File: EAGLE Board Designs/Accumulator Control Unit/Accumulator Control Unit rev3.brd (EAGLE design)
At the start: 186.7 x 135.7 mm, 237 parts, among them J1 CONNECTOR-CAN_μF_S_RA_, J2 CONNECTOR-8_MF_T_V_, J3 CONNECTOR-8_S_S, J4 CONNECTOR-2_MF_T_V_, J5 CONNECTOR-12_MF_T_V_, J6 CONNECTOR-14_MF_T_V_, J7 JUMPER_0603_, Q1 TRANSISTOR_N_MOS__PMV15ENEA, Q2 TRANSISTOR_N_MOS__PMV15ENEA, Q3 TRANSISTOR_N_MOS__PMV15ENEA, Q4 TRANSISTOR_N_MOS__PMV15ENEA, T1 TRANSFORMER_HM2112ZNLT_AIRGAP, U1 RELAY_SOLIDSTATE_NO, U10 OPAMP_1_CHANNEL_OPA991, U11 LOGICGATE_AND_DCK3, U12 OPAMP_1_CHANNEL_OPA991, U13 OPAMP_1_CHANNEL_OPA991, U14 OPAMP_1_CHANNEL_OPA991, U15 LOGICGATE_AND_DCK3, U16 RELAY_SOLIDSTATE_NO, U17 VOLTAGE_REGULATOR_SOT223_3.3V, U18 OPAMP_1_CHANNEL_OPA991, U19 MAX7404, U2 ADG1423, U20 OPAMP_1_CHANNEL_OPA991, U21 LOGICGATE_BUFFER, U22 OPAMP_1_CHANNEL_OPA991, U25 TCAN1051HQV-Q1, U26 MAX7404, U27 OPAMP_1_CHANNEL_OPA991, U28 MAX7404, U29 OPAMP_1_CHANNEL_OPA991, U3 LM555, U30 MAX7404, U4 OPAMP_1_CHANNEL_OPA991, U40 RELAY_SOLIDSTATE_NO, U5 LTC6820, U6 ADM8316WBX30, U7 OPAMP_1_CHANNEL_OPA991, U8 LOGICGATE_AND_DCK3, U9 OPAMP_1_CHANNEL_OPA991

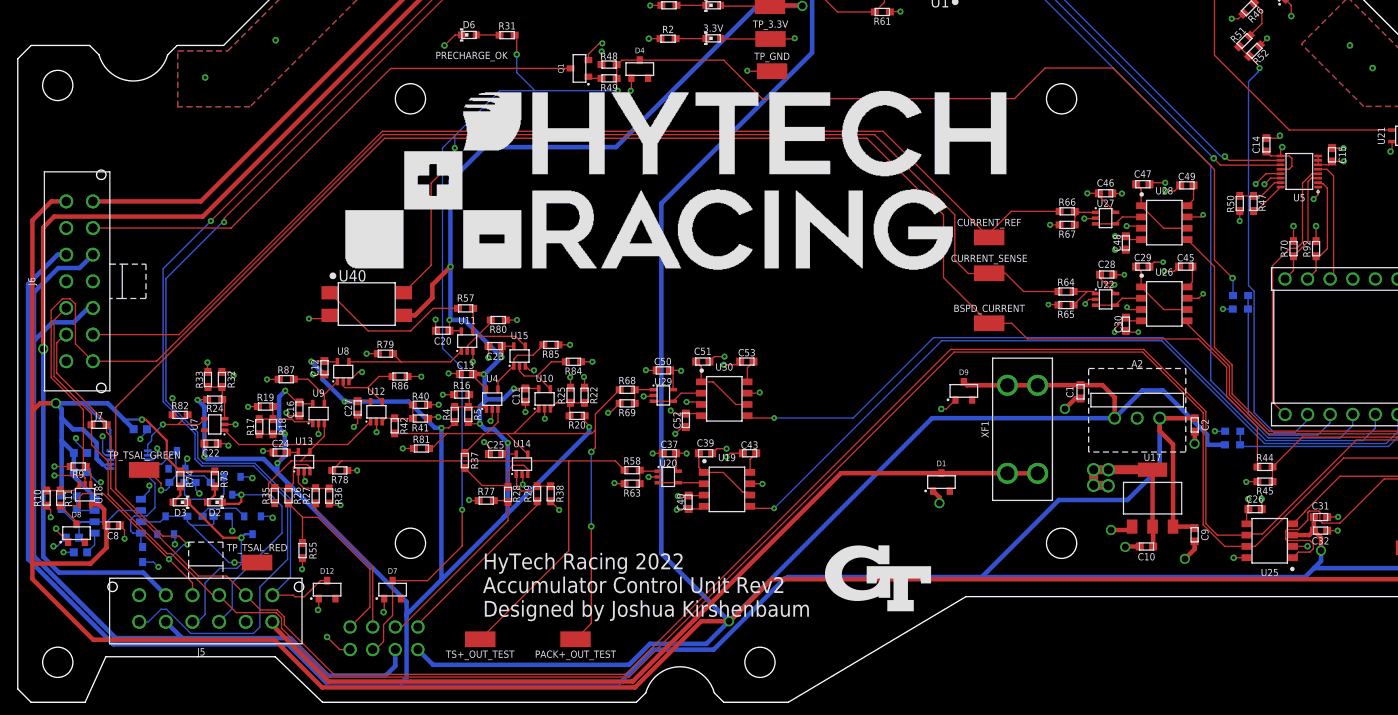
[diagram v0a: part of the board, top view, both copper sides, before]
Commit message: can jumper, tsal fuse
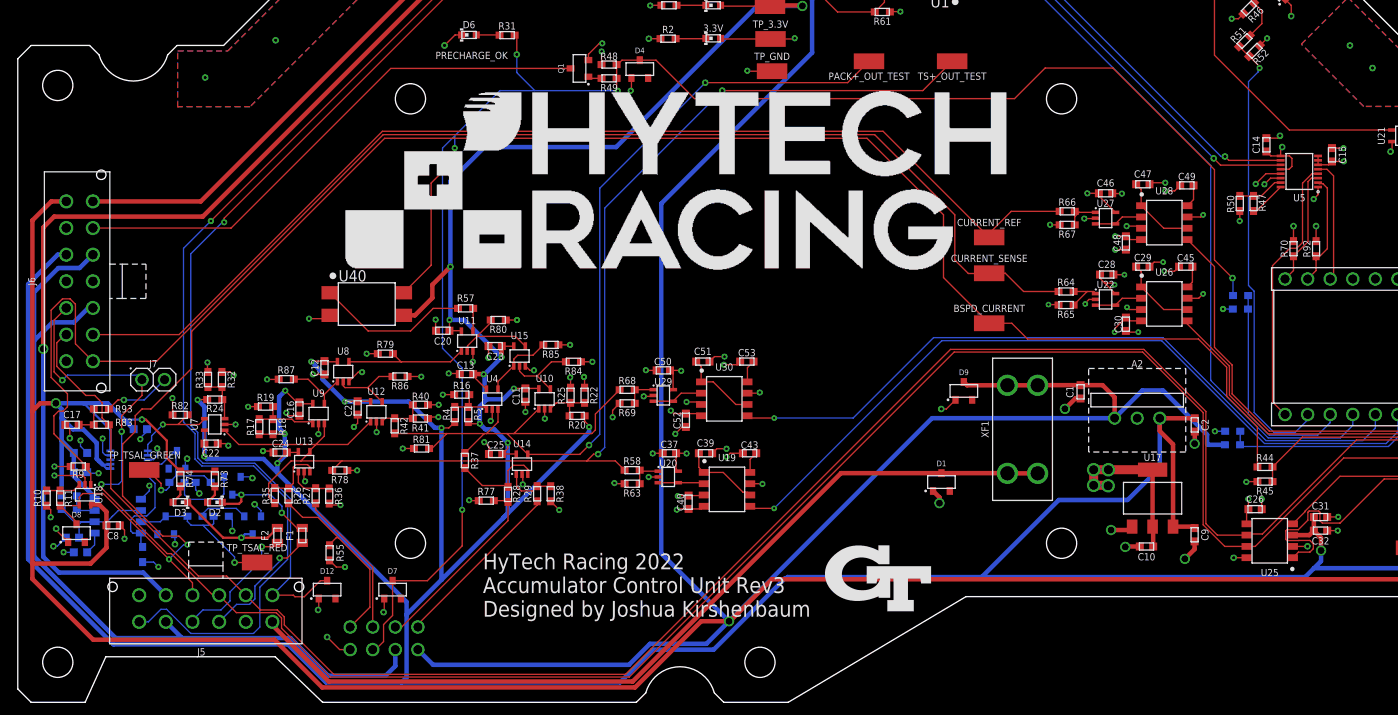
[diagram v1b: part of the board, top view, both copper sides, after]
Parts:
- added C17: CAPACITOR_0603_10V_4.7NF, HyTechDevices:0603-CAP
- added F1, F2: FUSE_0603_.75A, HyTechDevices:0603-FUSE
- added R83, R93: RESISTOR_0603_60.4, HyTechDevices:0603-RES
- J7: value JUMPER_0603_ -> JUMPER__1X02; device HyTechDevices:0603-RES -> HyTechDevices:1X02
- R14, R30, R39, R44, R51: value RESISTOR_0603_33K -> RESISTOR_0603_
- moved TS+_OUT_TEST 83.9 mm to (105.1, 70.6)
- moved PACK+_OUT_TEST 72.9 mm to (95.8, 70.6)
- moved J7 7.94 mm to (15.2, 34.8)
- moved R55 3.06 mm to (35.1, 15.3)
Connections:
- new net CANH/1.3B: J7.2, R93.2
- new net N$21: C17.2, R83.1, R93.1
- new net N$28: F1.1, J5.3
- new net N$31: F2.1, J5.4
- net CANL: now also R83.2; no longer J7.2
- net GND: now also C17.1
- net TSAL_GREEN: now also F1.2; no longer J5.3
- net TSAL_RED: now also F2.2; no longer J5.4
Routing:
- net TS+_OUT: track 93.2 -> 144.5 mm, vias 0 -> 2
- net PACK+_OUT: track 69.2 -> 117.7 mm
- net N$31: track 0.00 -> 14.8 mm, vias 0 -> 1
- net N$28: track 0.00 -> 14.1 mm, vias 0 -> 1
- net TSAL_GREEN: track 25.2 -> 13.0 mm, vias 1 -> 2
- net CANH: track 219.4 -> 230.1 mm, vias 0 -> 3
- net TSAL_RED: track 22.3 -> 13.6 mm
- net CANH/1.3B: track 0.00 -> 7.63 mm, vias 0 -> 1
- net N$21: track 0.00 -> 3.48 mm
- net IMD_OK: track 179.2 -> 176.9 mm
- net AMS_OK: track 216.0 -> 214.1 mm
- net CURRENT: track 161.7 -> 163.3 mm
- net GND: track 225.7 -> 227.2 mm, vias 164 -> 165
- net ISO_TS-: track 22.5 -> 21.0 mm
- net N$19: track 19.2 -> 18.3 mm
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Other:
- board text added: "HyTech Racing 2022 Accumulator Control Unit Rev3 Designed by Joshua Kirshenbaum"
- board text removed: "HyTech Racing 2022 Accumulator Control Unit Rev2 Designed by Joshua Kirshenbaum"

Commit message: fix text
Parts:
- removed D6: LED_0603_RED, HyTechDevices:0603-LED
- added PRECHARGE_OK: LED_0603_RED, HyTechDevices:0603-LED
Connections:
- net GND: now also PRECHARGE_OK.1; no longer D6.1
- net N$4: now also PRECHARGE_OK.2; no longer D6.2
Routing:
- net N$4: track 2.63 -> 4.41 mm
- net GND: track 227.2 -> 228.3 mm, vias 165 -> 145
- removed copper zone on layer 16, net GND
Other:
- board text removed: "PRECHARGE_OK"
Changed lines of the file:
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@@
 Accumulator Control Unit Rev3
 Designed by Joshua Kirshenbaum</text>
-<text x="46.99" y="70.866" size="0.8128" layer="25" font="vector" ratio="16">PRECHARGE_OK</text>
 </plain>
 <attributes>
@@
 <attribute name="VOLTAGE" value="8V" x="111.88109375" y="-5.19748125" size="1.778" layer="27" display="off"/>
 </element>
-<element name="D6" library="HyTechDevices" package="0603-LED" value="LED_0603_RED" x="50.75510625" y="73.57428125" smashed="yes">
-<attribute name="COLOR" value="Red" x="92.66510625" y="-14.05571875" size="1.778" layer="27" display="off"/>
-<attribute name="DKPN" value="754-1786-1-ND" x="92.66510625" y="-14.05571875" size="1.778" layer="27" display="off"/>
-<attribute name="MANUFACTURER" value="Kingbright" x="92.66510625" y="-14.05571875" size="1.778" layer="27" display="off"/>
-<attribute name="MOPN" value="604-APT1608SECKJ3PRV" x="92.66510625" y="-14.05571875" size="1.778" layer="27" display="off"/>
-<attribute name="MPN" value="APT1608SECK/J3-PRV" x="92.66510625" y="-14.05571875" size="1.778" layer="27" display="off"/>
-<attribute name="NAME" x="50.75510625" y="74.32428125" size="0.8128" layer="25" font="vector" align="bottom-center"/>
+<element name="PRECHARGE_OK" library="HyTechDevices" package="0603-LED" value="LED_0603_RED" x="48.97710625" y="73.57428125" smashed="yes">
+<attribute name="COLOR" value="Red" x="90.88710625" y="-14.05571875" size="1.778" layer="27" display="off"/>
+<attribute name="DKPN" value="754-1786-1-ND" x="90.88710625" y="-14.05571875" size="1.778" layer="27" display="off"/>
+<attribute name="MANUFACTURER" value="Kingbright" x="90.88710625" y="-14.05571875" size="1.778" layer="27" display="off"/>
+<attribute name="MOPN" value="604-APT1608SECKJ3PRV" x="90.88710625" y="-14.05571875" size="1.778" layer="27" display="off"/>
+<attribute name="MPN" value="APT1608SECK/J3-PRV" x="90.88710625" y="-14.05571875" size="1.778" layer="27" display="off"/>
+<attribute name="NAME" x="48.97710625" y="74.32428125" size="0.8128" layer="25" font="vector" align="bottom-center"/>
 </element>
 <element name="J1" library="HyTechDevices" package="MOLEX_MICROFIT_SMD_RIGHTANGLE_04_DUAL" value="CONNECTOR-CAN_μF_S_RA_" x="162.12229375" y="15.88451875" smashed="yes">
@@
 <attribute name="MOPN" value="603-RC0603FR-071KL" x="70.28770625" y="-21.70111875" size="1.778" layer="27" display="off"/>
 <attribute name="MPN" value="RC0603FR-071KL" x="70.28770625" y="-21.70111875" size="1.778" layer="27" display="off"/>
-<attribute name="NAME" x="55.04770625" y="74.18388125" size="0.8128" layer="25" font="vector" align="bottom-center"/>
+<attribute name="NAME" x="55.04770625" y="74.43788125" size="0.8128" layer="25" font="vector" align="bottom-center"/>
 <attribute name="POWER" value="0.1W" x="70.28770625" y="-21.70111875" size="1.778" layer="27" display="off"/>
 <attribute name="RESISTANCE" value="1k" x="70.28770625" y="-21.70111875" size="1.778" layer="27" display="off"/>
@@
 <contactref element="C20" pad="2"/>
 <contactref element="U11" pad="3"/>
-<contactref element="D6" pad="1"/>
+<contactref element="PRECHARGE_OK" pad="1"/>
 <contactref element="Q1" pad="2"/>
 <contactref element="D4" pad="1"/>
@@
 <vertex x="17.9832" y="65.4304"/>
 </polygon>
-<polygon width="0.1524" layer="16">
-<vertex x="40.386" y="125.3744"/>
-<vertex x="46.5328" y="125.3744"/>
-<vertex x="46.5582" y="125.349"/>
-<vertex x="46.5582" y="85.9282"/>
-<vertex x="26.1366" y="65.5066"/>
-<vertex x="17.9832" y="65.5066"/>
-<vertex x="17.9832" y="71.7804"/>
-<vertex x="23.622" y="71.7804"/>
-<vertex x="40.6908" y="88.8492"/>
-<vertex x="40.6908" y="125.0696"/>
-</polygon>
 <polygon width="0.1524" layer="1" isolate="0.3048">
 <vertex x="170.673" y="71.628"/>
@@
 <vertex x="155.8036" y="71.628"/>
 </polygon>
-<polygon width="0.1524" layer="16" isolate="0.3048">
-<vertex x="149.6314" y="77.7748"/>
-<vertex x="155.7782" y="71.628"/>
-<vertex x="170.6984" y="71.628"/>
-<vertex x="170.6984" y="65.532"/>
-<vertex x="151.4094" y="65.532"/>
-<vertex x="144.399" y="72.5424"/>
-</polygon>
 <polygon width="0.1524" layer="1" isolate="0.3048">
 <vertex x="185.4454" y="64.0588"/>
@@
 <vertex x="185.4454" y="18.3642"/>
 </polygon>
-<via x="43.4848" y="123.3678" extent="1-16" drill="0.35"/>
-<via x="43.6372" y="112.1664" extent="1-16" drill="0.35"/>
-<via x="43.6372" y="103.6066" extent="1-16" drill="0.35"/>
-<via x="43.7134" y="95.123" extent="1-16" drill="0.35"/>
-<via x="42.9768" y="87.63" extent="1-16" drill="0.35"/>
-<via x="36.6776" y="80.5942" extent="1-16" drill="0.35"/>
-<via x="29.0068" y="72.9742" extent="1-16" drill="0.35"/>
-<via x="21.082" y="68.7832" extent="1-16" drill="0.35"/>
-<via x="149.86" y="72.39" extent="1-16" drill="0.35"/>
-<via x="152.4" y="69.85" extent="1-16" drill="0.35"/>
-<via x="156.21" y="68.58" extent="1-16" drill="0.35"/>
-<via x="161.29" y="68.58" extent="1-16" drill="0.35"/>
-<via x="166.37" y="68.58" extent="1-16" drill="0.35"/>
-<polygon width="0.1524" layer="16" isolate="0.3048">
-<vertex x="185.4454" y="64.0588"/>
-<vertex x="185.4454" y="18.3388"/>
-<vertex x="178.2318" y="18.3388"/>
-<vertex x="178.2318" y="64.0588"/>
-</polygon>
-<via x="182.1942" y="60.452" extent="1-16" drill="0.35"/>
-<via x="182.3212" y="54.4322" extent="1-16" drill="0.35"/>
-<via x="182.5498" y="47.9298" extent="1-16" drill="0.35"/>
-<via x="182.4228" y="41.4528" extent="1-16" drill="0.35"/>
-<via x="182.4228" y="35.306" extent="1-16" drill="0.35"/>
-<via x="182.1942" y="29.3878" extent="1-16" drill="0.35"/>
-<via x="182.3212" y="23.0124" extent="1-16" drill="0.35"/>
 <contactref element="R84" pad="1"/>
 <contactref element="R85" pad="1"/>
@@
 <wire x1="41.2242" y1="8.7122" x2="41.148" y2="8.636" width="0.1524" layer="1"/>
 <via x="41.148" y="8.636" extent="1-16" drill="0.35"/>
-<wire x1="48.006" y1="72.39" x2="49.19028125" y2="73.57428125" width="0.1524" layer="1"/>
-<via x="48.006" y="72.39" extent="1-16" drill="0.35"/>
-<wire x1="49.19028125" y1="73.57428125" x2="49.93010625" y2="73.57428125" width="0.1524" layer="1"/>
+<wire x1="45.212" y1="72.136" x2="46.65028125" y2="73.57428125" width="0.1524" layer="1"/>
+<via x="45.212" y="72.136" extent="1-16" drill="0.35"/>
+<wire x1="46.65028125" y1="73.57428125" x2="48.15210625" y2="73.57428125" width="0.1524" layer="1"/>
 <contactref element="C17" pad="1"/>
 <wire x1="5.346" y1="29.718" x2="5.852365625" y2="29.211634375" width="0.1524" layer="1"/>
@@
 <signal name="N$4">
 <contactref element="R31" pad="1"/>
-<contactref element="D6" pad="2"/>
-<wire x1="51.58010625" y1="73.57428125" x2="54.17230625" y2="73.57428125" width="0.1524" layer="1"/>
+<contactref element="PRECHARGE_OK" pad="2"/>
+<wire x1="49.80210625" y1="73.57428125" x2="54.17230625" y2="73.57428125" width="0.1524" layer="1"/>
 <wire x1="54.17230625" y1="73.57428125" x2="54.19770625" y2="73.54888125" width="0.1524" layer="1"/>
 </signal>

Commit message: some changes based on checklist
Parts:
- removed C35: CAPACITOR_0603_10V_0.1UF, HyTechDevices - Copy:0603-CAP
- removed R13: RESISTOR_0603_100K, HyTechDevices - Copy:0603-RES
- removed R59: RESISTOR_0603_10K, HyTechDevices:0603-RES
- removed U$3: (no value), HyTechAesthetics:TS
- added PRECHARGE_OK_TEST: TEST_POINT, HyTechDevices - Copy:MICRO_MINIATURE
- added R94: RESISTOR_0603_10K, HyTechDevices:0603-RES
- added U$2: (no value), HyTechAesthetics:HV_0.50"
- R53: value RESISTOR_0603_100 -> RESISTOR_0603_120
- moved U$12 16.5 mm to (100.9, 16.4)
- moved U$18 16.5 mm to (100.9, 66.4)
- moved PACK+_OUT_TEST 2.03 mm to (93.7, 70.6)
- moved C36 1.78 mm to (161.5, 62.1)
- moved R55 0.66 mm to (35.1, 16.0), turned to 0 degrees
- renumbered D2 to TSAL_GREEN, D3 to TSAL_RED
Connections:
- removed net N$15: R13.2, U21.2, U6.1
- net +3V3: no longer C35.1, U6.5
- net AMS_OK_3.3V: now also U6.1; no longer U21.4
- net GND: no longer C35.2, R13.1, R59.1
- net PRECHARGE_OK: now also PRECHARGE_OK_TEST.1
- net TEENSY_OK: now also R94.1, R94.2, U6.5; no longer R59.2
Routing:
- net TEENSY_OK: track 30.8 -> 52.3 mm
- net N$15: track 19.6 -> 0.00 mm
- net AMS_OK_3.3V: track 60.9 -> 78.8 mm, vias 0 -> 2
- net PRECHARGE_OK: track 207.0 -> 216.6 mm
- net GND: track 228.3 -> 223.7 mm, vias 145 -> 142
- net +3V3: track 86.6 -> 82.5 mm, vias 25 -> 24
- net PACK+_OUT: track 117.7 -> 115.7 mm
- removed copper zone on layer 1, net GND

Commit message: passed review
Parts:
- removed C40, C47, C48, C51: CAPACITOR_0603_10V_0.1UF, HyTechDevices - Copy:0603-CAP
- removed C43, C45, C49, C53: CAPACITOR_0603_10V_680PF, HyTechDevices - Copy:0603-CAP
- removed C46, C50: CAPACITOR_0603_25V_0.1UF, HyTechDevices:0603-CAP
- removed D12: TVS_15V, HyTechDevices:SOT-23
- removed J7: JUMPER__1X02, HyTechDevices:1X02
- removed R82, R84, R85, R86, R87: RESISTOR_0603_10K, HyTechDevices - Copy:0603-RES
- removed R83, R93: RESISTOR_0603_60.4, HyTechDevices:0603-RES
- removed R92: RESISTOR_0603_2K, HyTechDevices:0603-RES
- removed R94: RESISTOR_0603_10K, HyTechDevices:0603-RES
- removed U$21, U$22: (no value), HyTechManufacturing:MOUNTING_M3
- removed U28, U30: MAX7404, HyTechDevices:SOIC-08(NARROW,0.15")
- removed U29: OPAMP_1_CHANNEL_OPA991, HyTechDevices:SC-70-5
- removed U40: RELAY_SOLIDSTATE_NO, HyTechDevices:DIP-4
- added C100: CAPACITOR_0603_10V_10NF, HyTechDevices - Copy:0603-CAP
- added C101: CAPACITOR_0603_25V_1UF, HyTechDevices - Copy:0603-CAP
- added C102: CAPACITOR_0603_25V_0.1UF, HyTechDevices - Copy:0603-CAP
- added C103: CAPACITOR_0603_10V_4.7UF, HyTechDevices - Copy:0603-CAP
- added C104: CAPACITOR_0603_25V_1UF, HyTechDevices:0603-CAP
- added C18, C19, C34, C38: CAPACITOR_0603_10V_0.1UF, HyTechDevices:0603-CAP
- added C35: CAPACITOR_0603_25V_0.1UF, HyTechDevices:0603-CAP
- added D3: TVS_15V, HyTechDevices:SOT-23
- added J100: CONNECTOR-8_S_S, HyTechDevices:FLEX_STACK_PTH_08_DUAL
- added R100, R59: RESISTOR_0603_10K, HyTechDevices - Copy:0603-RES
- added R105: RESISTOR_0603_43K, HyTechDevices:0603-RES
- added R106: RESISTOR_0603_1K, HyTechDevices:0603-RES
- added R107: RESISTOR_0603_12K, HyTechDevices - Copy:0603-RES
- added R108, R110: RESISTOR_0603_, HyTechDevices:0603-RES
- added R109: RESISTOR_0603_18.7K, HyTechDevices:0603-RES
- added R13: RESISTOR_0603_10, HyTechDevices:0603-RES
- added U$100: (no value), HyTechManufacturing:HV_LARGE
- added U$3: (no value), HyTechAesthetics:TS
- added U100: ADG1423, HyTechDevices:MSOP-10
- added U101: LM555, HyTechDevices:SOIC-08(NARROW,0.15")
- added U23, U24: OPAMP_1_CHANNEL_OPA991, HyTechDevices:SC-70-5
- A1: value TEENSY_4.0 -> VOLTAGE_REGULATOR_MODULE_OKI-78SR_5V; device HyTechDevices:TEENSY_SHORT -> HyTechDevices - Copy:OKI-78SR
- A2: value VOLTAGE_REGULATOR_MODULE_OKI-78SR_5V -> TEENSY_4.0; device HyTechDevices - Copy:OKI-78SR -> HyTechDevices:TEENSY_SHORT
- C1: value CAPACITOR_0603_25V_10UF -> CAPACITOR_0603_10V_10NF; device HyTechDevices:0603-CAP -> HyTechDevices - Copy:0603-CAP
- C10: value CAPACITOR_0603_10V_4.7UF -> CAPACITOR_0603_10V_0.1UF
- C11, C22, C31: device HyTechDevices:0603-CAP -> HyTechDevices - Copy:0603-CAP
- C12, C23: value CAPACITOR_0603_10V_0.1UF -> CAPACITOR_0603_10V_680PF; device HyTechDevices:0603-CAP -> HyTechDevices - Copy:0603-CAP
- C15: value CAPACITOR_0603_10V_10NF -> CAPACITOR_0603_10V_0.1UF
- C17: value CAPACITOR_0603_10V_4.7NF -> CAPACITOR_0603_10V_0.1UF
- C2: value CAPACITOR_0603_25V_10UF -> CAPACITOR_0603_25V_0.1UF
- C20: value CAPACITOR_0603_10V_0.1UF -> CAPACITOR_0603_25V_0.1UF
- C24: value CAPACITOR_0603_10V_0.1UF -> CAPACITOR_0603_25V_10UF
- C25: value CAPACITOR_0603_10V_0.1UF -> CAPACITOR_0603_10V_4.7NF
- C28, C7: value CAPACITOR_0603_25V_0.1UF -> CAPACITOR_0603_10V_0.1UF
- C29: value CAPACITOR_0603_10V_0.1UF -> CAPACITOR_0603_25V_0.1UF; device HyTechDevices - Copy:0603-CAP -> HyTechDevices:0603-CAP
- C3: value CAPACITOR_0603_25V_1UF -> CAPACITOR_0603_10V_0.1UF; device HyTechDevices:0603-CAP -> HyTechDevices - Copy:0603-CAP
- C32: value CAPACITOR_0603_10V_1UF -> CAPACITOR_0603_10V_680PF; device HyTechDevices:0603-CAP -> HyTechDevices - Copy:0603-CAP
- C33: value CAPACITOR_0603_10V_10NF -> CAPACITOR_0603_25V_10UF; device HyTechDevices - Copy:0603-CAP -> HyTechDevices:0603-CAP
- C36: value CAPACITOR_0603_10V_0.1UF -> CAPACITOR_0603_10V_4.7UF
- C37: value CAPACITOR_0603_25V_0.1UF -> CAPACITOR_0603_10V_1UF; device HyTechDevices:0603-CAP -> HyTechDevices - Copy:0603-CAP
- C39: value CAPACITOR_0603_10V_0.1UF -> CAPACITOR_0603_10V_1UF; device HyTechDevices - Copy:0603-CAP -> HyTechDevices:0603-CAP
- C4: value CAPACITOR_0603_10V_10NF -> CAPACITOR_0603_10V_680PF
- C5: value CAPACITOR_0603_10V_4.7UF -> CAPACITOR_0603_10V_0.1UF; device HyTechDevices - Copy:0603-CAP -> HyTechDevices:0603-CAP
- C6: value CAPACITOR_0603_25V_1UF -> CAPACITOR_0603_10V_10NF; device HyTechDevices - Copy:0603-CAP -> HyTechDevices:0603-CAP
- C9: value CAPACITOR_0603_10V_1UF -> CAPACITOR_0603_10V_0.1UF
- D1: value TVS_15V -> LED_0603_YELLOW; device HyTechDevices:SOT-23 -> HyTechDevices - Copy:0603-LED
- D10: value LED_0603_GREEN -> TVS_15V; device HyTechDevices:0603-LED -> HyTechDevices:SOT-23
- D11: value LED_0603_YELLOW -> TVS_15V; device HyTechDevices - Copy:0603-LED -> HyTechDevices:SOT-23
- D5: value TVS_15V -> LED_0603_GREEN; device HyTechDevices:SOT-23 -> HyTechDevices:0603-LED
- J1: value CONNECTOR-CAN_μF_S_RA_ -> CONNECTOR-2_MF_T_V_; device HyTechDevices:MOLEX_MICROFIT_SMD_RIGHTANGLE_04_DUAL -> HyTechDevices - Copy:MOLEX_MICROFIT_PTH_VERTICAL_02_SINGLE
- J3: value CONNECTOR-8_S_S -> CONNECTOR-14_MF_T_V_; device HyTechDevices:FLEX_STACK_PTH_08_DUAL -> HyTechDevices - Copy:MOLEX_MICROFIT_PTH_VERTICAL_14_DUAL
- J4: value CONNECTOR-2_MF_T_V_ -> JUMPER__1X02; device HyTechDevices - Copy:MOLEX_MICROFIT_PTH_VERTICAL_02_SINGLE -> HyTechDevices:1X02
- J6: value CONNECTOR-14_MF_T_V_ -> CONNECTOR-CAN_μF_S_RA_; device HyTechDevices - Copy:MOLEX_MICROFIT_PTH_VERTICAL_14_DUAL -> HyTechDevices:MOLEX_MICROFIT_SMD_RIGHTANGLE_04_DUAL
- R1: value RESISTOR_0603_1K -> RESISTOR_0603_120
- R10: device HyTechDevices - Copy:0603-RES -> HyTechDevices:0603-RES
- R11: value RESISTOR_0603_1.4K -> RESISTOR_0603_1K; device HyTechDevices - Copy:0603-RES -> HyTechDevices:0603-RES
- R14: value RESISTOR_0603_ -> RESISTOR_0603_10K
- R15: value RESISTOR_0603_12K -> RESISTOR_0603_2.2K
- R16, R19: value RESISTOR_0603_10.2K -> RESISTOR_0603_1K
- R17: value RESISTOR_0603_4.12K -> RESISTOR_0603_10K
- R18: value RESISTOR_0603_DNP -> RESISTOR_0603_10
- R2, R7: value RESISTOR_0603_1K -> RESISTOR_0603_2K
- R20: value RESISTOR_0603_11.5K -> RESISTOR_0603_
- R21: value RESISTOR_0603_10 -> RESISTOR_0603_15K
- R22: value RESISTOR_0603_DNP -> RESISTOR_0603_10K; device HyTechDevices:0603-RES -> HyTechDevices - Copy:0603-RES
- R23: value RESISTOR_0603_18.7K -> RESISTOR_0603_12K; device HyTechDevices:0603-RES -> HyTechDevices - Copy:0603-RES
- R24: value RESISTOR_0603_84.5K -> RESISTOR_0603_1K; device HyTechDevices:0603-RES -> HyTechDevices - Copy:0603-RES
- R25: value RESISTOR_0603_11.5K -> RESISTOR_0603_1K; device HyTechDevices:0603-RES -> HyTechDevices - Copy:0603-RES
- R26, R27: value RESISTOR_0603_11.5K -> RESISTOR_0603_10K
- R28: value RESISTOR_0603_11.5K -> RESISTOR_0603_470
- R29: value RESISTOR_0603_11.5K -> RESISTOR_0603_10K; device HyTechDevices:0603-RES -> HyTechDevices - Copy:0603-RES
- R30, R44: value RESISTOR_0603_ -> RESISTOR_0603_10K; device HyTechDevices:0603-RES -> HyTechDevices - Copy:0603-RES
- R31: value RESISTOR_0603_1K -> RESISTOR_0603_12K; device HyTechDevices:0603-RES -> HyTechDevices - Copy:0603-RES
- R32: value RESISTOR_0603_DNP -> RESISTOR_0603_2K
- R33: value RESISTOR_0603_11.5K -> RESISTOR_0603_2K
- R34: value RESISTOR_0603_2K -> RESISTOR_0603_470
- R35: value RESISTOR_0603_10.5K -> RESISTOR_0603_470; device HyTechDevices:0603-RES -> HyTechDevices - Copy:0603-RES
- R36: value RESISTOR_0603_10.5K -> RESISTOR_0603_60.4
- R37: value RESISTOR_0603_10.5K -> RESISTOR_0603_10K; device HyTechDevices:0603-RES -> HyTechDevices - Copy:0603-RES
- R38: value RESISTOR_0603_10.5K -> RESISTOR_0603_11.5K
- R39: value RESISTOR_0603_ -> RESISTOR_0603_84.5K
- R4: value RESISTOR_0603_DNP -> RESISTOR_0603_
- R41: value RESISTOR_0603_215K -> RESISTOR_0603_10.2K
- R42: value RESISTOR_0603_11.3K -> RESISTOR_0603_10K; device HyTechDevices:0603-RES -> HyTechDevices - Copy:0603-RES
- R43, R69: value RESISTOR_0603_12K -> RESISTOR_0603_10K
- R45: value RESISTOR_0603_12K -> RESISTOR_0603_DNP; device HyTechDevices - Copy:0603-RES -> HyTechDevices:0603-RES
- R46: value RESISTOR_0603_2.2K -> RESISTOR_0603_215K; device HyTechDevices - Copy:0603-RES -> HyTechDevices:0603-RES
- R47: value RESISTOR_0603_1K -> RESISTOR_0603_DNP; device HyTechDevices - Copy:0603-RES -> HyTechDevices:0603-RES
- R48: value RESISTOR_0603_10K -> RESISTOR_0603_10.2K
- R49: value RESISTOR_0603_10 -> RESISTOR_0603_4.12K
- R5: value RESISTOR_0603_4.12K -> RESISTOR_0603_12K; device HyTechDevices:0603-RES -> HyTechDevices - Copy:0603-RES
- R50: value RESISTOR_0603_1K -> RESISTOR_0603_10K
- R51: value RESISTOR_0603_ -> RESISTOR_0603_11.5K
- R52: value RESISTOR_0603_15K -> RESISTOR_0603_10K; device HyTechDevices:0603-RES -> HyTechDevices - Copy:0603-RES
- R53: value RESISTOR_0603_120 -> RESISTOR_0603_11.5K
- R54: value RESISTOR_0603_10K -> RESISTOR_0603_DNP
- R56: value RESISTOR_0603_2K -> RESISTOR_0603_12K; device HyTechDevices:0603-RES -> HyTechDevices - Copy:0603-RES
- R57: value RESISTOR_0603_470 -> RESISTOR_0603_1K; device HyTechDevices:0603-RES -> HyTechDevices - Copy:0603-RES
- R58: value RESISTOR_0603_10K -> RESISTOR_0603_1.4K
- R6: value RESISTOR_0603_43K -> RESISTOR_0603_10K
- R60: value RESISTOR_0603_10K -> RESISTOR_0603_60.4; device HyTechDevices - Copy:0603-RES -> HyTechDevices:0603-RES
- R61, R62: value RESISTOR_0603_10K -> RESISTOR_0603_2K
- R63: value RESISTOR_0603_12K -> RESISTOR_0603_4.12K; device HyTechDevices - Copy:0603-RES -> HyTechDevices:0603-RES
- R64: value RESISTOR_0603_10K -> RESISTOR_0603_DNP; device HyTechDevices - Copy:0603-RES -> HyTechDevices:0603-RES
- R65: value RESISTOR_0603_12K -> RESISTOR_0603_10.5K; device HyTechDevices - Copy:0603-RES -> HyTechDevices:0603-RES
- R66: value RESISTOR_0603_10K -> RESISTOR_0603_11.5K; device HyTechDevices - Copy:0603-RES -> HyTechDevices:0603-RES
- R67: value RESISTOR_0603_12K -> RESISTOR_0603_11.5K; device HyTechDevices - Copy:0603-RES -> HyTechDevices:0603-RES
- R68: value RESISTOR_0603_10K -> RESISTOR_0603_10.5K; device HyTechDevices - Copy:0603-RES -> HyTechDevices:0603-RES
- R70: value RESISTOR_0603_2K -> RESISTOR_0603_11.3K
- R71: value RESISTOR_0603_1K -> RESISTOR_0603_10K; device HyTechDevices:0603-RES -> HyTechDevices - Copy:0603-RES
- R72: value RESISTOR_0603_2K -> RESISTOR_0603_10.5K
- R73: value RESISTOR_0603_2K -> RESISTOR_0603_10K; device HyTechDevices:0603-RES -> HyTechDevices - Copy:0603-RES
- R74: value RESISTOR_0603_2K -> RESISTOR_0603_11.5K
- R75: value RESISTOR_0603_470 -> RESISTOR_0603_11.5K; device HyTechDevices - Copy:0603-RES -> HyTechDevices:0603-RES
- R76: value RESISTOR_0603_470 -> RESISTOR_0603_10.5K; device HyTechDevices - Copy:0603-RES -> HyTechDevices:0603-RES
- R78, R80: value RESISTOR_0603_10K -> RESISTOR_0603_12K
- R79: value RESISTOR_0603_10K -> RESISTOR_0603_; device HyTechDevices - Copy:0603-RES -> HyTechDevices:0603-RES
- R8: value RESISTOR_0603_1K -> RESISTOR_0603_2K; device HyTechDevices:0603-RES -> HyTechDevices - Copy:0603-RES
- R9: value RESISTOR_0603_10K -> RESISTOR_0603_1K; device HyTechDevices - Copy:0603-RES -> HyTechDevices:0603-RES
- U$1, U$5: device HyTechAesthetics:GLV -> HyTechManufacturing:MOUNTING_M3
- U$10, U$9: device HyTechAesthetics:TS -> HyTechManufacturing:MOUNTING_M3
- U$13: device HyTechManufacturing:MOUNTING_M3 -> HyTechManufacturing:LOGO_HYTECH_EXTRA_LARGE
- U$15: device HyTechManufacturing:LOGO_HYTECH_EXTRA_LARGE -> HyTechAesthetics:LOGO_GT_0.50"
- U$16: device HyTechAesthetics:LOGO_GT_0.50" -> HyTechManufacturing:MOUNTING_M3
- U$2: device HyTechAesthetics:HV_0.50" -> HyTechAesthetics:GLV
- U$4: device HyTechAesthetics:HV_0.50" -> HyTechManufacturing:HV_LARGE
- U$6: device HyTechManufacturing:MOUNTING_M3 -> HyTechAesthetics:TS
- U$7: device HyTechManufacturing:MOUNTING_M3 -> HyTechAesthetics:GLV
- U10, U4: value OPAMP_1_CHANNEL_OPA991 -> MAX7404; device HyTechDevices:SC-70-5 -> HyTechDevices:SOIC-08(NARROW,0.15")
- U11, U15: value LOGICGATE_AND_DCK3 -> OPAMP_1_CHANNEL_OPA991
- U12, U14: value OPAMP_1_CHANNEL_OPA991 -> LOGICGATE_AND_DCK3
- U16: value RELAY_SOLIDSTATE_NO -> LOGICGATE_AND_DCK3; device HyTechDevices:DIP-4 -> HyTechDevices:SC-70-5
- U17: value VOLTAGE_REGULATOR_SOT223_3.3V -> OPAMP_1_CHANNEL_OPA991; device HyTechDevices - Copy:SOT223 -> HyTechDevices:SC-70-5
- U2: value ADG1423 -> RELAY_SOLIDSTATE_NO; device HyTechDevices:MSOP-10 -> HyTechDevices:DIP-4
- U21: value LOGICGATE_BUFFER -> OPAMP_1_CHANNEL_OPA991
- U25: value TCAN1051HQV-Q1 -> MAX7404
- U26: value MAX7404 -> VOLTAGE_REGULATOR_SOT223_3.3V; device HyTechDevices:SOIC-08(NARROW,0.15") -> HyTechDevices - Copy:SOT223
- U27: value OPAMP_1_CHANNEL_OPA991 -> TCAN1051HQV-Q1; device HyTechDevices:SC-70-5 -> HyTechDevices:SOIC-08(NARROW,0.15")
- U3: value LM555 -> OPAMP_1_CHANNEL_OPA991; device HyTechDevices:SOIC-08(NARROW,0.15") -> HyTechDevices:SC-70-5
- U6: value ADM8316WBX30 -> LOGICGATE_BUFFER; device HyTechDevices:SOT-23-5 -> HyTechDevices:SC-70-5
- U7: value OPAMP_1_CHANNEL_OPA991 -> ADM8316WBX30; device HyTechDevices:SC-70-5 -> HyTechDevices:SOT-23-5
- U8: value LOGICGATE_AND_DCK3 -> RELAY_SOLIDSTATE_NO; device HyTechDevices:SC-70-5 -> HyTechDevices:DIP-4
- moved U$8 185.4 mm to (4.50, 67.9)
- moved C7 158.5 mm to (161.5, 62.1), flipped to the top, turned to 90 degrees
- moved J6 156.6 mm to (162.1, 15.9), turned to 0 degrees
- moved U7 149.0 mm to (168.1, 59.9), turned to 180 degrees
- moved U$14 147.3 mm to (44.2, 16.4)
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- renumbered C52 to C21, D13 to D2, D14 to D6, D15 to D100, D16 to D101, Q3 to Q100, Q4 to Q101, R88 to R103, R89 to R101, R90 to R104, R91 to R102, TP6 to TP2, TP7 to TP1
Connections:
- new net N$95: C7.1, R27.2, U7.3
- net +12V: now also A1.1, C101.1, C102.1, C104.1, C24.1, C35.1, D7.3, J100.5, J3.7, J6.1, R106.2, R108.1, R61.1, R62.1, R7.2, U100.1, U100.2, U100.5, U101.8, U2.4, U20.5; no longer A2.1, C1.1, C3.1, C6.1, C7.1, C8.1, D9.3, J1.1, J3.5, J6.7, R3.2, R39.1, R56.2, R73.1, R74.1, U16.4, U18.5, U2.1, U2.2, U2.5, U3.8
- net +3V3: now also A2.3.3V, C2.1, C20.1, C29.1, C34.2, C36.1, C5.1, C6.2, C8.1, C9.1, R32.2, R33.2, U10.4, U10.7, U18.5, U24.5, U25.4, U25.7, U26.2, U3.5, U4.4, U4.7, U6.5, U9.5; no longer A1.3.3V, C14.1, C15.2, C26.2, C28.1, C37.1, C40.1, C46.1, C48.1, C50.1, R70.2, R92.2, U17.2, U17.4, U20.5, U21.5, U22.5, U25.5, U26.7, U28.4, U28.7, U29.5, U30.4, U30.7
- net +5V: now also A1.3, A2.VIN, C14.1, C15.1, C17.1, C18.1, C19.1, C26.1, C28.1, C33.1, C37.1, C38.2, C39.2, J3.5, R39.2, R47.2, R49.2, R53.2, R63.2, R64.2, U16.5, U17.5, U21.5, U22.5, U23.5, U26.3, U27.3, U8.4; no longer A1.VIN, A2.3, C11.1, C12.1, C2.1, C20.1, C22.1, C23.1, C24.1, C25.1, C31.2, C32.2, C9.1, J6.5, R17.2, R18.2, R20.2, R24.2, R4.2, R5.2, U10.5, U17.3, U25.3, U4.5, U40.4, U7.5, U8.5, U9.5
- net 0.5989V_DIV: now also R38.2, R39.1, R40.2, U21.3; no longer R24.1, R32.2, R33.2, U7.3
- net 0.95X_DIV: now also R45.2, R46.2, R70.1, U13.3; no longer R40.2, R41.2, R42.1, U12.3
- net 12VIN: now also D8.3; no longer D1.3
- net 12V_SCALED_3.3V: now also A2.D19, R107.1, R108.2; no longer A1.D19, R39.2, R43.1
- net 2.5_DIV: now also R51.2, R53.1, R54.2, U17.3; no longer R20.1, R22.2, R25.2, U10.3
- net 3.56V_DIV_A: now also R41.2, R63.1, R64.1, U11.1; no longer R17.1, R18.1, R19.2, U9.1
- net 3.56V_DIV_B: now also R47.1, R48.2, R49.1, U15.1; no longer R16.2, R4.1, R5.1, U4.1
- net 60V_THRESHOLD: now also R37.2, U100.6, U100.7, U21.4; no longer R82.2, U2.6, U2.7, U7.4
- net ACCUMULATOR_GND: now also J3.14; no longer J6.14
- net AIR2-: now also J3.13, Q2.3; no longer J6.13, Q1.3
- net AMS_OK: now also R12.2, U2.3; no longer R61.2, U1.3
- net AMS_OK_3.3V: now also R13.1, R14.1, U7.1; no longer R21.1, R54.1, U6.1
- net BSPD_CURRENT: now also D9.3, R58.2, R79.1, U20.4; no longer D8.3, R11.2, R44.1, U18.4
- net BSPD_CURRENT_TEENSY: now also A2.D22, R79.2, R80.1; no longer A1.D22, R44.2, R45.1
- net CANH: now also J3.3, J4.1, J6.4, U27.7; no longer J1.4, J6.3, J7.1, U25.7
- net CANH/1.3B: now also J4.2, R36.2; no longer J7.2, R93.2
- net CANL: now also J3.2, J6.3, R60.2, U27.6; no longer J1.3, J6.2, R83.2, U25.6
- net CS_LTC_6820: now also A2.D10; no longer A1.D10
- net CURRENT: now also J3.8, R30.1, R59.2, U20.1; no longer J6.8, R64.1, R9.2, U18.1
- net CURRENT_BUFFER: now also U10.2, U9.3, U9.4; no longer U22.3, U22.4, U26.2
- net CURRENT_FILTERED: now also A2.D21, U10.5; no longer A1.D21, U26.5
- net CURRENT_REF: now also J3.9, R22.1; no longer J6.9, R66.1
- net CURRENT_REF_BUFFER: now also U3.3, U3.4, U4.2; no longer U27.3, U27.4, U28.2
- net CURRENT_REF_FILTERED: now also A2.D20, U4.5; no longer A1.D20, U28.5
- net GND: now also A1.2, A2.AGND/GND, A2.GND, C100.2, C101.2, C102.2, C103.2, C104.2, C15.2, C17.2, C18.2, C19.2, C25.1, C26.2, C31.2, C32.2, C34.1, C35.2, C38.1, C39.1, C6.1, D11.1, D3.1, J100.8, J3.11, J3.4, J3.6, J6.2, R100.1, R107.2, R11.1, R110.2, R14.2, R15.1, R17.2, R21.2, R23.2, R24.2, R26.1, R29.1, R3.1, R31.2, R37.1, R38.1, R42.1, R43.1, R44.1, R45.1, R48.1, R5.2, R50.1, R51.1, R52.1, R54.1, R56.2, R57.1, R59.1, R6.1, R68.2, R69.1, R73.1, R76.2, R78.2, R80.2, U1.2, U10.3, U100.4, U100.8, U101.1, U11.2, U12.3, U14.3, U15.2, U16.3, U17.2, U21.2, U23.2, U24.2, U25.3, U26.1, U27.8, U3.2, U4.3, U6.3, U8.2; no longer A1.AGND/GND, A1.GND, A2.2, C15.1, C17.1, C25.2, C26.1, C31.1, C32.1, C39.2, C40.2, C43.2, C45.2, C46.2, C47.2, C48.2, C49.2, C50.2, C51.2, C53.2, C6.2, D1.1, D12.1, J1.2, J3.8, J6.11, J6.4, J6.6, R1.1, R15.2, R16.1, R22.1, R25.1, R30.2, R32.1, R33.1, R36.2, R38.2, R43.2, R45.2, R48.2, R50.2, R52.2, R54.2, R55.1, R60.1, R61.1, R62.1, R63.2, R65.2, R67.2, R69.2, R7.1, R72.1, R77.1, R78.1, R79.1, R8.1, R80.1, R82.1, R84.1, R85.1, R86.1, R87.1, U10.2, U11.3, U12.2, U14.2, U15.3, U16.2, U17.1, U2.4, U2.8, U21.3, U25.2, U25.8, U26.3, U28.3, U29.2, U3.1, U30.3, U4.2, U40.2, U6.2, U8.3
- net HV+_OUT_OK: now also R43.2, U12.4, U14.1; no longer R79.2, U11.1, U8.4
- net IMD_OK: now also D10.3, R4.1, R6.2, U1.3; no longer D12.3, R14.1, R62.2, U16.3
- net IMD_OK_TEENSY: now also A2.D16, R4.2, R5.1; no longer A1.D16, R14.2, R15.1
- net ISO_PACK+: now also J100.1, R75.1; no longer J3.1, R29.1
- net ISO_PACK-: now also J100.2, R73.2, R74.1; no longer J3.2, R28.1, R77.2
- net ISO_TS+: now also J100.3, R67.1; no longer J3.3, R27.1
- net ISO_TS-: now also J100.4, R66.1, R81.2; no longer J3.4, R26.1, R55.2
- net MHS: now also D3.3, R15.2, R20.1; no longer D5.3, R46.2, R51.1
- net MHS_TEENSY: now also A2.D14, R20.2, R21.1; no longer A1.D14, R51.2, R52.1
- net N$1: now also R19.2; no longer R2.2
- net N$10: now also R67.2, R68.1, U22.1; no longer R27.2, R36.1, U13.1
- net N$11: now also R65.1, R66.2, U22.3; no longer R26.2, R35.1, U13.3
- net N$12: now also R57.2, R58.1, U20.3; no longer R10.2, R11.1, U18.3
- net N$13: now also A2.D11, R33.1; no longer A1.D11, R92.1
- net N$14: now also R11.2; no longer R71.2
- net N$16: now also R7.1, U2.1; no longer R56.1, U1.1
- net N$17: now also R3.2; no longer R7.2
- net N$18: now also U100.9; no longer U2.9
- net N$19: now also U101.3; no longer U3.3
- net N$2: now also R10.2; no longer R1.2
- net N$20: now also Q1.3, U2.2; no longer Q2.3, U1.2
- net N$21: now also C25.2, R36.1, R60.1; no longer C17.2, R83.1, R93.1
- net N$22: now also R75.2, R76.1, U23.1; no longer R29.2, R38.1, U14.1
- net N$23: now also R72.1, R74.2, U23.3; no longer R28.2, R37.1, U14.3
- net N$24: now also R62.2; no longer R73.2
- net N$25: now also A2.D0, A2.D4, U27.4; no longer A1.D0, A1.D4, U25.4
- net N$26: now also C31.1, U25.1, U25.6; no longer C39.1, U19.1, U19.6
- net N$27: now also R2.2; no longer R72.2
- net N$28: now also F2.1; no longer F1.1
- net N$29: now also A2.D1, A2.D3, U27.1; no longer A1.D1, A1.D3, U25.1
- net N$3: now also C103.1, R105.1, U101.2, U101.6; no longer C5.1, R6.1, U3.2, U3.6
- net N$30: now also Q1.1, R13.2; no longer Q2.1, R21.2
- net N$31: now also F1.1; no longer F2.1
- net N$36: now also R25.1; no longer R47.1
- net N$37: now also R24.1, R25.2; no longer R47.2, R50.1
- net N$39: now also C1.1; no longer C33.1
- net N$4: now also R16.1; no longer R31.1
- net N$41: now also R28.1, U14.4; no longer R57.1, U11.4
- net N$43: now also A2.D12, R32.1; no longer A1.D12, R70.1
- net N$44: now also A2.D13; no longer A1.D13
- net N$45: now also C32.1, U25.8; no longer C43.1, U19.8
- net N$46: now also R61.2; no longer R74.2
- net N$47: now also D5.2, R34.1; no longer D10.2, R75.1
- net N$48: now also R77.2, R78.1, U24.1; no longer R58.2, R63.1, U20.1
- net N$49: now also R28.2, U8.1; no longer R57.2, U40.1
- net N$5: now also C100.1, U101.5; no longer C4.1, U3.5
- net N$50: now also C11.1, U10.1, U10.6; no longer C29.1, U26.1, U26.6
- net N$51: now also C12.1, U10.8; no longer C45.1, U26.8
- net N$52: now also R30.2, R31.1, U9.1; no longer R64.2, R65.1, U22.1
- net N$53: now also C3.1, U4.1, U4.6; no longer C47.1, U28.1, U28.6
- net N$54: now also C4.1, U4.8; no longer C49.1, U28.8
- net N$55: now also R22.2, R23.1, U3.1; no longer R66.2, R67.1, U27.1
- net N$56: now also C22.1, U19.1, U19.6; no longer C51.1, U30.1, U30.6
- net N$57: now also C23.1, U19.8; no longer C53.1, U30.8
- net N$58: now also R55.2, R56.1, U18.1; no longer R68.2, R69.1, U29.1
- net N$59: now also R35.1; no longer R76.1
- net N$6: now also R105.2, R106.1, U101.7; no longer R3.1, R6.2, U3.7
- net N$7: now also Q2.1, R18.2; no longer Q1.1, R49.2
- net N$8: now also R8.2, U1.1; no longer R34.2, U16.1
- net N$9: now also D1.1, R9.2; no longer D11.1, R8.2
- net OKHS: now also D1.2, R8.1; no longer D11.2, R34.1
- net PACK+_BUFFER: now also U18.3, U18.4, U19.2; no longer U29.3, U29.4, U30.2
- net PACK+_FILTERED: now also A2.D17, U19.5; no longer A1.D17, U30.5
- net PACK+_OUT: now also R55.1, R70.2, R71.2, R72.2, U15.3, U17.1, U23.4; no longer R37.2, R42.2, R68.1, R81.2, U10.1, U14.4, U4.3
- net PRECHARGE+_OUT_OK: now also R29.2, U14.2, U16.4; no longer R80.2, U11.2, U15.4
- net PRECHARGE_OK: now also D11.3, J100.7, R109.1, R16.2, R17.1, R18.1, U8.3; no longer D7.3, J3.7, R23.1, R31.2, R48.1, R49.1, U40.3
- net PRECHARGE_OK_TEENSY: now also A2.D15, R109.2, R110.1; no longer A1.D15, R23.2, R30.1
- net PRECHARGE_REACHED: now also R44.2, U12.2, U13.4; no longer R86.2, U12.4, U8.2
- net SHDN: now also J100.6, J3.10, J3.12; no longer J3.6, J6.10, J6.12
- net TD+: now also J1.1, R1.2; no longer J4.1, R53.2
- net TD-: now also J1.2, R1.1; no longer J4.2, R53.1
- net TEENSY_OK: now also A2.D6, R27.1, R35.2, U7.5; no longer A1.D6, C36.1, R76.2, R94.1, R94.2, U6.3, U6.5
- net TIMER_EN: now also R100.2, U100.10, U101.4; no longer R60.2, U2.10, U3.4
- net TS+_OUT: now also R65.2, R69.2, R77.1, U11.3, U13.1, U21.1, U22.4; no longer R35.2, R58.1, R78.2, U12.1, U13.4, U7.1, U9.3
- net TS+_OUT_BUFFER: now also U24.3, U24.4, U25.2; no longer U19.2, U20.3, U20.4
- net TS+_OUT_FILTERED: now also A2.D18, U25.5; no longer A1.D18, U19.5
- net TS+_OUT_OV_OK: now also R42.2, U11.4, U12.1; no longer R87.2, U8.1, U9.4
- net TSAL_GREEN: now also F2.2; no longer F1.2
- net TSAL_RED: now also F1.2; no longer F2.2
- net V_PACK_REF_OV_OK: now also R50.2, U15.4, U16.1; no longer R85.2, U15.1, U4.4
- net V_PACK_REF_UV_OK: now also R52.2, U16.2, U17.4; no longer R84.2, U10.4, U15.2
- net WATCHDOG_INPUT: now also A2.D5, R26.2, R34.2, U7.4; no longer A1.D5, R12.2, R75.2, U6.4
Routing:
- net BSPD_CURRENT: track 211.9 -> 246.7 mm, vias 2 -> 4
- net CURRENT: track 163.3 -> 186.0 mm, vias 0 -> 2
- net CURRENT_REF: track 124.6 -> 135.6 mm, vias 0 -> 2
- net TEENSY_OK: track 52.3 -> 44.9 mm
- net IMD_OK_TEENSY: track 106.6 -> 113.5 mm
- net IP: track 87.5 -> 93.6 mm
- net N$95: track 0.00 -> 5.64 mm
- net IM: track 92.5 -> 98.1 mm
- net PRECHARGE_OK: track 216.6 -> 211.7 mm
- net TS+_OUT: track 144.5 -> 141.7 mm
- net AMS_OK_3.3V: track 78.8 -> 77.6 mm, vias 2 -> 0
- net PACK+_OUT: track 115.7 -> 114.7 mm

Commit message: added new changes based on doc
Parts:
- removed C7: CAPACITOR_0603_10V_0.1UF, HyTechDevices - Copy:0603-CAP
- removed D5: LED_0603_GREEN, HyTechDevices:0603-LED
- removed D6: LED_0603_RED, HyTechDevices:0603-LED
- added R82: RESISTOR_0603_10K, HyTechDevices:0603-RES
- added TEENSY_OK: LED_0603_RED, HyTechDevices:0603-LED
- added WATCHDOG: LED_0603_GREEN, HyTechDevices:0603-LED
- moved WATCHDOG_OK 34.0 mm to (148.2, 72.9)
- moved U6 6.11 mm to (153.9, 68.1), turned to 0 degrees
- moved R27 3.45 mm to (161.8, 63.2)
- moved U7 3.45 mm to (164.8, 61.0)
- moved R26 3.45 mm to (160.7, 58.6)
- moved CURRENT_REF 3.30 mm to (111.3, 71.9)
- moved CURRENT_SENSE 3.05 mm to (120.2, 71.9)
- moved BSPD_CURRENT 3.05 mm to (129.3, 71.9)
- moved PACK+_OUT_TEST 0.76 mm to (93.0, 71.9)
- moved TS+_OUT_TEST 0.76 mm to (102.6, 71.9)
- renumbered D1 to OKHS, TP1 to TD-, TP2 to TD+
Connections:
- new net N$15: R82.2, U6.2, U7.1
- net AMS_OK_3.3V: now also U6.4; no longer U7.1
- net GND: now also R82.1, TEENSY_OK.1, WATCHDOG.1; no longer C7.2, D5.1, D6.1
- net N$47: now also WATCHDOG.2; no longer D5.2
- net N$59: now also TEENSY_OK.2; no longer D6.2
- net N$95: no longer C7.1
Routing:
- net WATCHDOG_INPUT: track 32.5 -> 59.3 mm
- net N$59: track 1.53 -> 20.7 mm
- net AMS_OK_3.3V: track 77.6 -> 59.3 mm
- net N$47: track 1.53 -> 19.2 mm
- net N$15: track 0.00 -> 17.3 mm, vias 0 -> 2
- net N$95: track 5.64 -> 2.10 mm
- net CURRENT: track 186.0 -> 189.0 mm
- net CURRENT_REF: track 135.6 -> 138.3 mm
- net GND: track 223.7 -> 225.5 mm, vias 142 -> 141
- net BSPD_CURRENT: track 246.7 -> 248.3 mm
- net +3V3: track 82.5 -> 83.4 mm
- net TS+_OUT: track 141.7 -> 142.5 mm
- net PACK+_OUT: track 114.7 -> 115.4 mm
- net TEENSY_OK: track 44.9 -> 45.5 mm
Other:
- outline, holes or cut-outs redrawn
- board text added: "HyTech Racing 2022 Accumulator Control Unit Rev3 Designed by Joshua Kirshenbaum, Liwei Sun, Zekun Li"
- board text removed: "HyTech Racing 2022 Accumulator Control Unit Rev3 Designed by Joshua Kirshenbaum"
